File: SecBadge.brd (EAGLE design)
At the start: 69 x 43 mm, 21 parts, among them J1 USB_A, U1 32U4, Y1 16MHz

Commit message: Added button designator in schematic.
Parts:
- S2: value (none) -> BUTTON_1
- S3: value (none) -> BUTTON_2
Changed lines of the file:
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@@
 <layer number="23" name="tOrigins" color="15" fill="1" visible="yes" active="yes"/>
 <layer number="24" name="bOrigins" color="15" fill="1" visible="yes" active="yes"/>
-<layer number="25" name="tNames" color="7" fill="1" visible="yes" active="yes"/>
+<layer number="25" name="tNames" color="7" fill="1" visible="no" active="yes"/>
 <layer number="26" name="bNames" color="7" fill="1" visible="no" active="yes"/>
 <layer number="27" name="tValues" color="7" fill="1" visible="no" active="yes"/>
@@
 <element name="R5" library="ZnibbLib" package="1206" value="90" x="17.78" y="14.24"/>
 <element name="S1" library="ZnibbLib" package="DIP8" value="DIP-SW" x="58.42" y="8.89"/>
-<element name="S2" library="SparkFun-Switches" package="TACTILE_SWITCH_PTH_6.0MM" value="" x="63.5" y="27.94">
+<element name="S2" library="SparkFun-Switches" package="TACTILE_SWITCH_PTH_6.0MM" value="BUTTON_1" x="63.5" y="27.94">
 <attribute name="SF_SKU" value="COM-00097" x="63.5" y="27.94" size="1.778" layer="27" display="off"/>
 <attribute name="PROD_ID" value=" SWCH-08441" x="63.5" y="27.94" size="1.778" layer="27" display="off"/>
 </element>
-<element name="S3" library="SparkFun-Switches" package="TACTILE_SWITCH_PTH_6.0MM" value="" x="63.5" y="20.32">
+<element name="S3" library="SparkFun-Switches" package="TACTILE_SWITCH_PTH_6.0MM" value="BUTTON_2" x="63.5" y="20.32">
 <attribute name="SF_SKU" value="COM-00097" x="63.5" y="20.32" size="1.778" layer="27" display="off"/>
 <attribute name="PROD_ID" value=" SWCH-08441" x="63.5" y="20.32" size="1.778" layer="27" display="off"/>

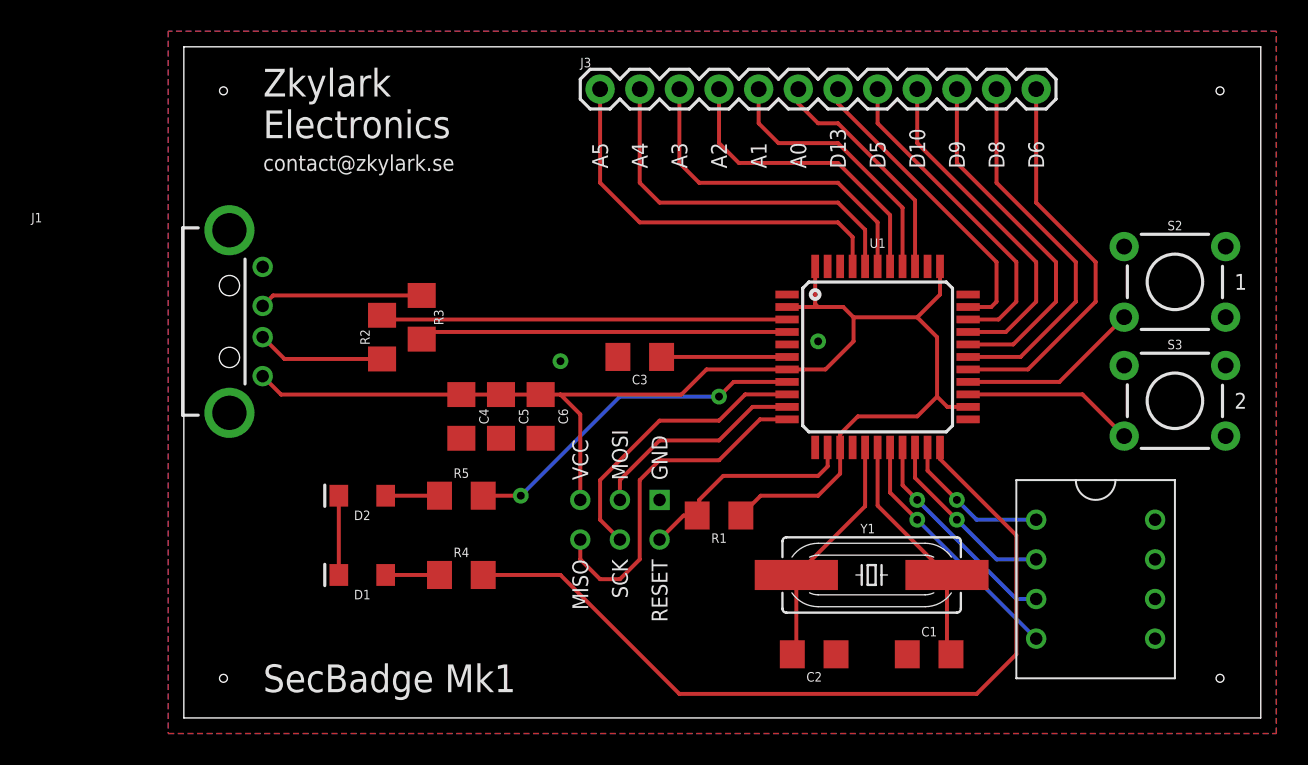
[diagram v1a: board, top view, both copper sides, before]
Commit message: Added VCC and GND to expansion header.
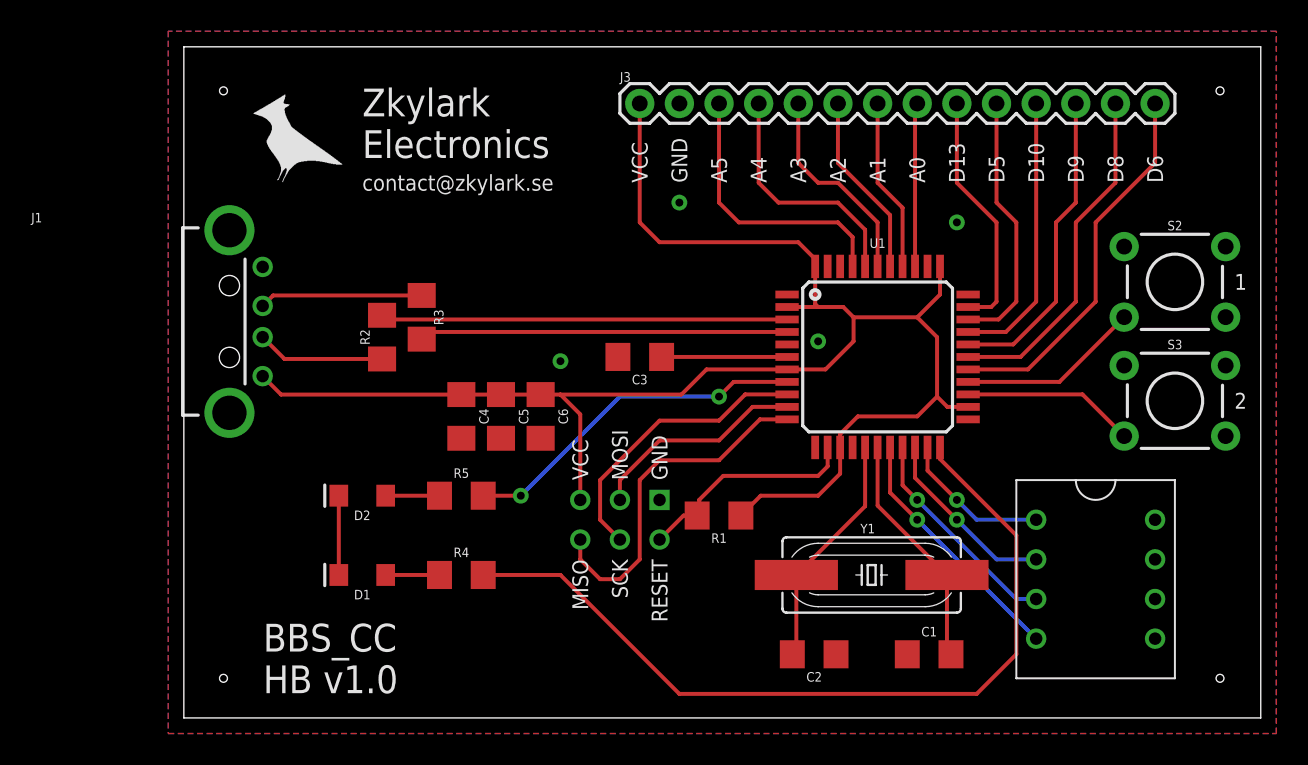
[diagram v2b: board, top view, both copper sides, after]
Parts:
- J3: device SparkFun-Connectors:1X12 -> SparkFun-Connectors:1X14
- moved J3 2.70 mm to (29.2, 39.4)
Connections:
- net 5V: now also J3.1
- net A0: now also J3.8; no longer J3.6
- net A1: now also J3.7; no longer J3.5
- net A2: now also J3.6; no longer J3.4
- net A3: now also J3.5; no longer J3.3
- net A4: now also J3.4; no longer J3.2
- net A5: now also J3.3; no longer J3.1
- net D10: now also J3.11; no longer J3.9
- net D13: now also J3.9; no longer J3.7
- net D5: now also J3.10; no longer J3.8
- net D6: now also J3.14; no longer J3.12
- net D8: now also J3.13; no longer J3.11
- net D9: now also J3.12; no longer J3.10
- net GND: now also J3.2
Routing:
- net 5V: track 88.8 -> 109.1 mm
- net A4: track 24.0 -> 15.5 mm
- net A3: track 21.8 -> 13.3 mm
- net A5: track 25.5 -> 17.7 mm
- net A2: track 19.6 -> 11.8 mm
- net A1: track 17.4 -> 11.1 mm
- net A0: track 15.2 -> 10.5 mm
- net D13: track 19.8 -> 15.7 mm
- net D5: track 20.9 -> 16.8 mm
- net D10: track 21.9 -> 17.9 mm
- net D9: track 23.0 -> 20.0 mm
- net D8: track 24.1 -> 22.1 mm
- net D6: track 25.2 -> 24.2 mm
- net GND: vias 2 -> 4
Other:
- board text added: "BBS_CC HB v1.0"
- board text removed: "SecBadge Mk1"

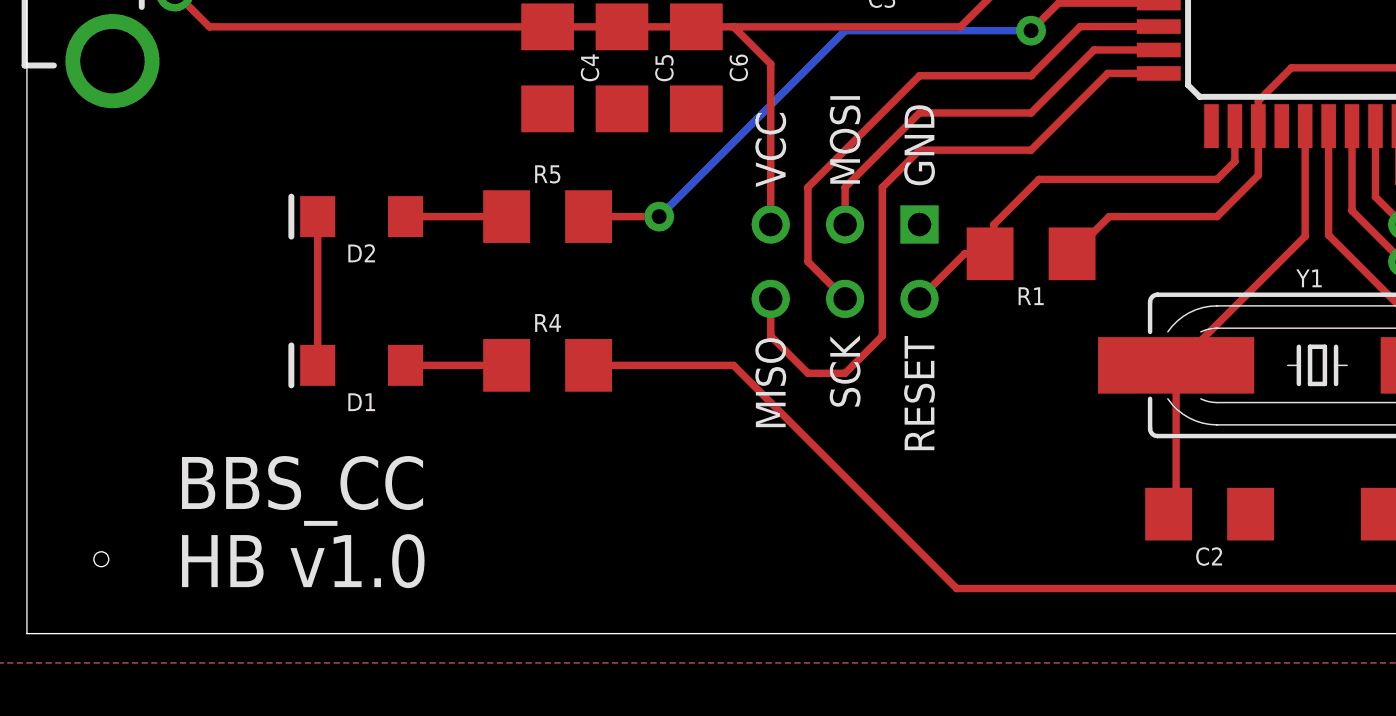
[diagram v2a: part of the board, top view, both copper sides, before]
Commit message: Updated board silkscreen info.
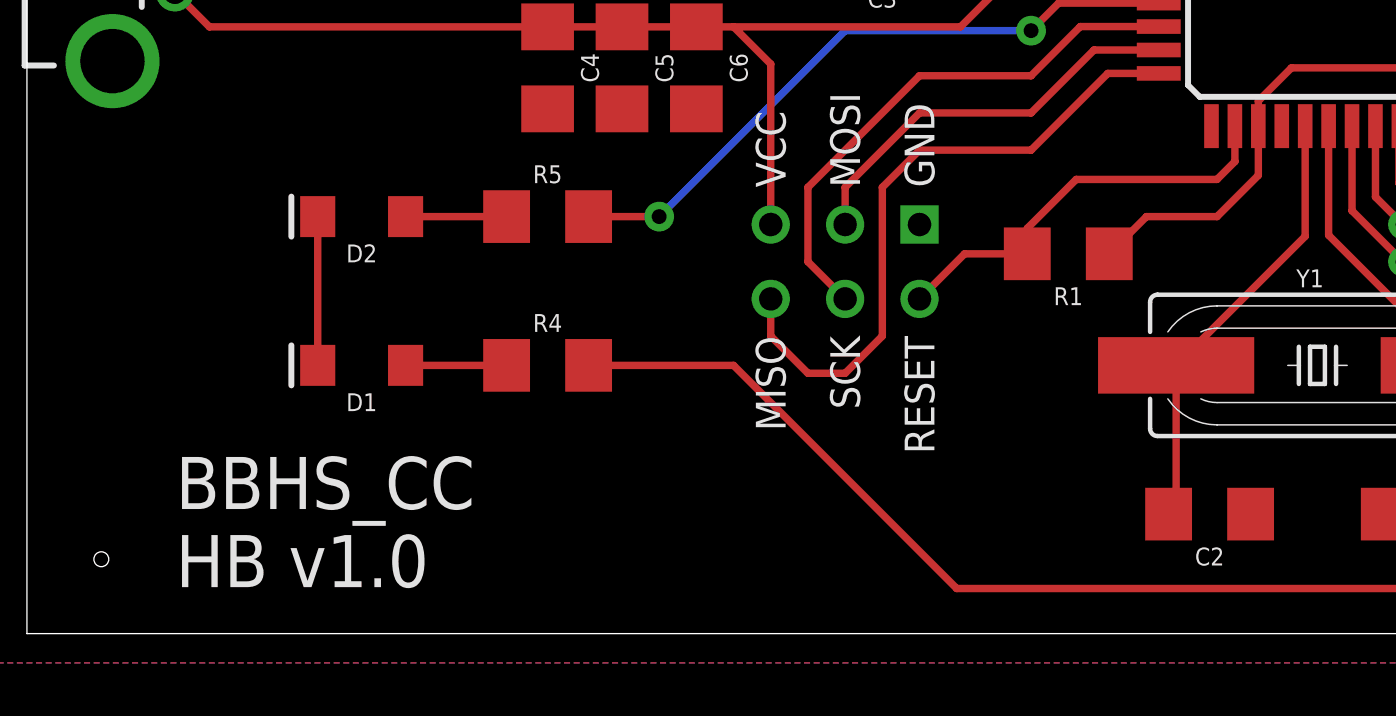
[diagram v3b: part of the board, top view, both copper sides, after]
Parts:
- moved R1 1.27 mm to (35.6, 13.0)
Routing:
- net 5V: track 109.1 -> 107.9 mm
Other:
- board text added: "BBHS_CC HB v1.0"
- board text removed: "BBS_CC HB v1.0"
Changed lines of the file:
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@@
 <text x="67.31" y="27.94" size="1.016" layer="21" font="vector" ratio="15" align="center-left">1</text>
 <text x="67.31" y="20.32" size="1.016" layer="21" font="vector" ratio="15" align="center-left">2</text>
-<text x="5.08" y="3.81" size="1.778" layer="21" font="vector" ratio="15" align="center-left">BBS_CC
+<text x="5.08" y="3.81" size="1.778" layer="21" font="vector" ratio="15" align="center-left">BBHS_CC
 HB v1.0</text>
 <text x="34.29" y="34.29" size="1.016" layer="21" ratio="15" rot="R90" align="center-left">A5</text>
@@
 <element name="D2" library="ZnibbLib" package="LED-1206" value="GREEN" x="11.43" y="14.24" rot="R180"/>
 <element name="J2" library="ZnibbLib" package="3X2_NO_SILK" value="" x="27.94" y="12.7" rot="R90"/>
-<element name="R1" library="ZnibbLib" package="1206" value="10k" x="34.29" y="12.97" rot="R180"/>
+<element name="R1" library="ZnibbLib" package="1206" value="10k" x="35.56" y="12.97" rot="R180"/>
 <element name="R2" library="ZnibbLib" package="1206" value="22" x="12.7" y="24.4" smashed="yes" rot="R270">
 <attribute name="NAME" x="11.303" y="24.4" size="0.6096" layer="25" font="vector" ratio="20" rot="R270" align="bottom-center"/>
@@
 <wire x1="31.88" y1="20.72" x2="24.13" y2="20.72" width="0.254" layer="1"/>
 <wire x1="24.13" y1="20.72" x2="22.86" y2="20.72" width="0.254" layer="1"/>
-<wire x1="40.64" y1="14.24" x2="36.96" y2="14.24" width="0.254" layer="1"/>
-<wire x1="36.96" y1="14.24" x2="35.69" y2="12.97" width="0.254" layer="1"/>
+<wire x1="40.64" y1="14.24" x2="38.23" y2="14.24" width="0.254" layer="1"/>
+<wire x1="38.23" y1="14.24" x2="36.96" y2="12.97" width="0.254" layer="1"/>
 <contactref element="J1" pad="VBUS"/>
 <wire x1="17.78" y1="20.72" x2="6.231" y2="20.72" width="0.254" layer="1"/>
@@
 <wire x1="41.25" y1="17.33" x2="41.25" y2="16.12" width="0.254" layer="1"/>
 <wire x1="41.25" y1="16.12" x2="40.64" y2="15.51" width="0.254" layer="1"/>
-<wire x1="40.64" y1="15.51" x2="34.56" y2="15.51" width="0.254" layer="1"/>
-<wire x1="34.56" y1="15.51" x2="33.02" y2="13.97" width="0.254" layer="1"/>
-<wire x1="33.02" y1="13.97" x2="33.02" y2="13.1" width="0.254" layer="1"/>
-<wire x1="33.02" y1="13.1" x2="32.89" y2="12.97" width="0.254" layer="1"/>
-<wire x1="32.89" y1="12.97" x2="32.02" y2="12.97" width="0.254" layer="1"/>
+<wire x1="40.64" y1="15.51" x2="35.83" y2="15.51" width="0.254" layer="1"/>
+<wire x1="34.16" y1="12.97" x2="32.02" y2="12.97" width="0.254" layer="1"/>
 <wire x1="32.02" y1="12.97" x2="30.48" y2="11.43" width="0.254" layer="1"/>
+<wire x1="35.83" y1="15.51" x2="34.16" y2="13.84" width="0.254" layer="1"/>
+<wire x1="34.16" y1="13.84" x2="34.16" y2="12.97" width="0.254" layer="1"/>
 </signal>
 <signal name="LED_RED">
